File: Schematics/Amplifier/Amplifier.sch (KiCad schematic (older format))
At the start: 38 parts, among them J1 Conn_01x03_Female, J2 Conn_01x03_Female, J3 Conn_01x03_Female, J4 Conn_01x03_Female, Q1 BD139, Q2 BD138, Q3 BD139, Q4 BD138, U1 NE5532

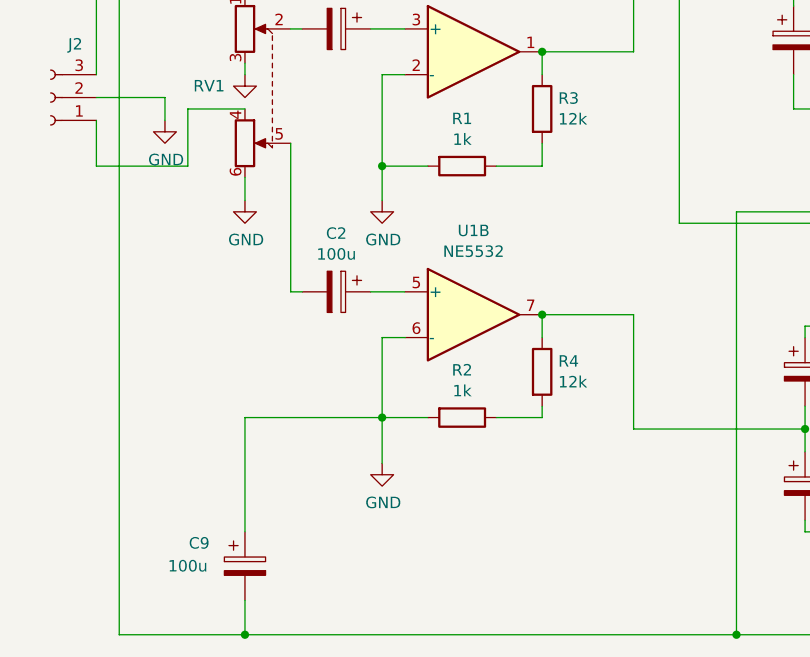
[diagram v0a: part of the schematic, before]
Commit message: Continue Amp schematic/PCB
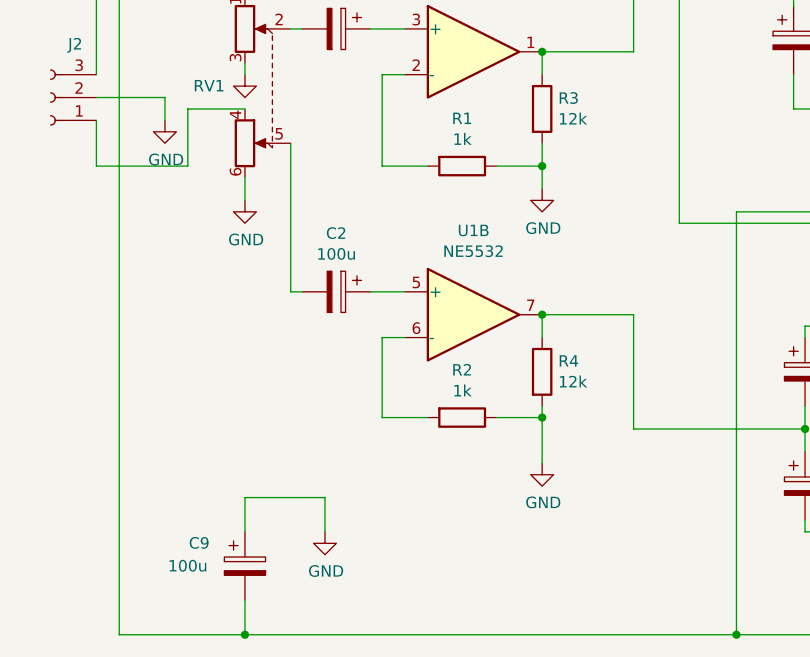
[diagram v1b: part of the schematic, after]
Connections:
- net GND: now also R1.1, R2.1, R3.2, R4.2; no longer R1.2, R2.2, U1.2 (-), U1.6 (-)
- new net: R1.2, U1.2 (-)
- new net: R2.2, U1.6 (-)
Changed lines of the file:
@@
 L power:GND #PWR05
 U 1 1 5E42E1F8
-P 3150 4250
-F 0 "#PWR05" H 3150 4000 50  0001 C CNN
-F 1 "GND" H 3155 4077 50  0000 C CNN
-F 2 "" H 3150 4250 50  0001 C CNN
-F 3 "" H 3150 4250 50  0001 C CNN
-	1    3150 4250
-	1    0    0    -1
-$EndComp
-Wire Wire Line
-	3150 4250 3150 4100
-Connection ~ 3150 4100
+P 3850 4200
+F 0 "#PWR05" H 3850 3950 50  0001 C CNN
+F 1 "GND" H 3855 4027 50  0000 C CNN
+F 2 "" H 3850 4200 50  0001 C CNN
+F 3 "" H 3850 4200 50  0001 C CNN
+	1    3850 4200
+	1    0    0    -1
+$EndComp
 $Comp
 L power:GND #PWR06
 U 1 1 5E42EEAA
-P 3150 5400
-F 0 "#PWR06" H 3150 5150 50  0001 C CNN
-F 1 "GND" H 3155 5227 50  0000 C CNN
-F 2 "" H 3150 5400 50  0001 C CNN
-F 3 "" H 3150 5400 50  0001 C CNN
-	1    3150 5400
-	1    0    0    -1
-$EndComp
-Wire Wire Line
-	3150 5400 3150 5200
-Connection ~ 3150 5200
+P 3850 5400
+F 0 "#PWR06" H 3850 5150 50  0001 C CNN
+F 1 "GND" H 3855 5227 50  0000 C CNN
+F 2 "" H 3850 5400 50  0001 C CNN
+F 3 "" H 3850 5400 50  0001 C CNN
+	1    3850 5400
+	1    0    0    -1
+$EndComp
 Wire Wire Line
 	1900 2600 2300 2600
@@
 Wire Wire Line
 	2550 6150 4700 6150
-Wire Wire Line
-	2550 5700 2550 5200
-Wire Wire Line
-	2550 5200 3150 5200
 $Comp
 L Connector:Screw_Terminal_01x03 J4
@@
 	4050 2500 4050 2800
 Connection ~ 3700 2800
+Wire Wire Line
+	3850 4100 3850 4200
+Connection ~ 3850 4100
+Wire Wire Line
+	3850 5200 3850 5400
+Connection ~ 3850 5200
+$Comp
+L power:GND #PWR?
+U 1 1 5E450109
+P 2900 5700
+F 0 "#PWR?" H 2900 5450 50  0001 C CNN
+F 1 "GND" H 2905 5527 50  0000 C CNN
+F 2 "" H 2900 5700 50  0001 C CNN
+F 3 "" H 2900 5700 50  0001 C CNN
+	1    2900 5700
+	1    0    0    -1
+$EndComp
+Wire Wire Line
+	2550 5700 2550 5550
+Wire Wire Line
+	2550 5550 2900 5550
+Wire Wire Line
+	2900 5550 2900 5700
 $EndSCHEMATC
